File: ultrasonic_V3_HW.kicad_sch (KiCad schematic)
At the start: 7 parts, among them J1 Conn_02x20_Odd_Even, J4 Conn_01x07_Pin, J5 Screw_Terminal_01x02

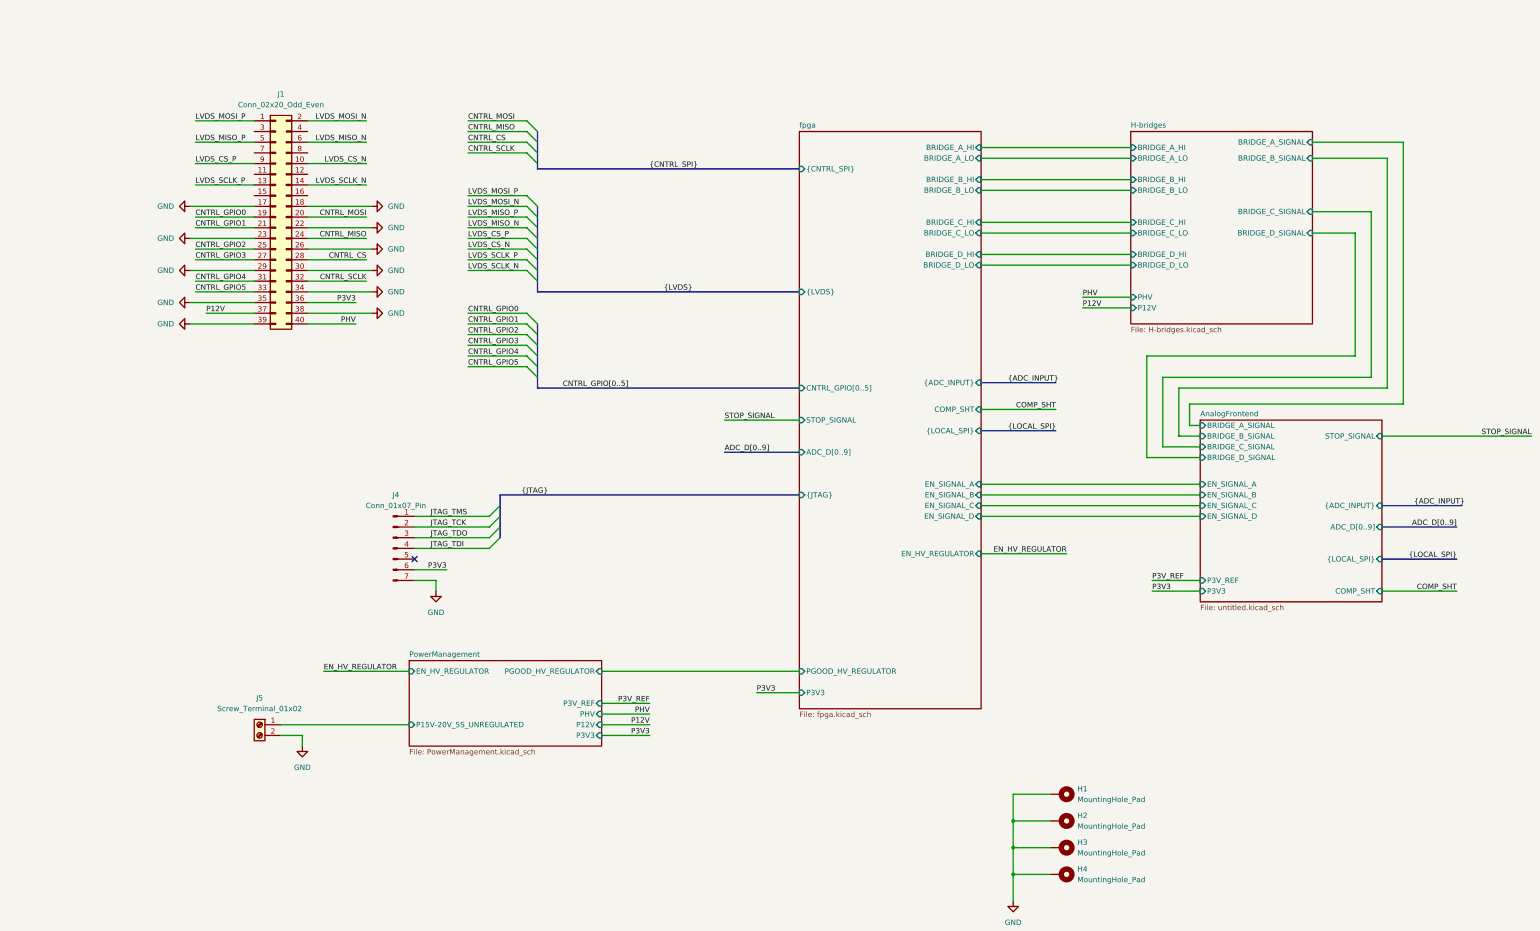
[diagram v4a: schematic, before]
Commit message: no errors schematic, basic routing done
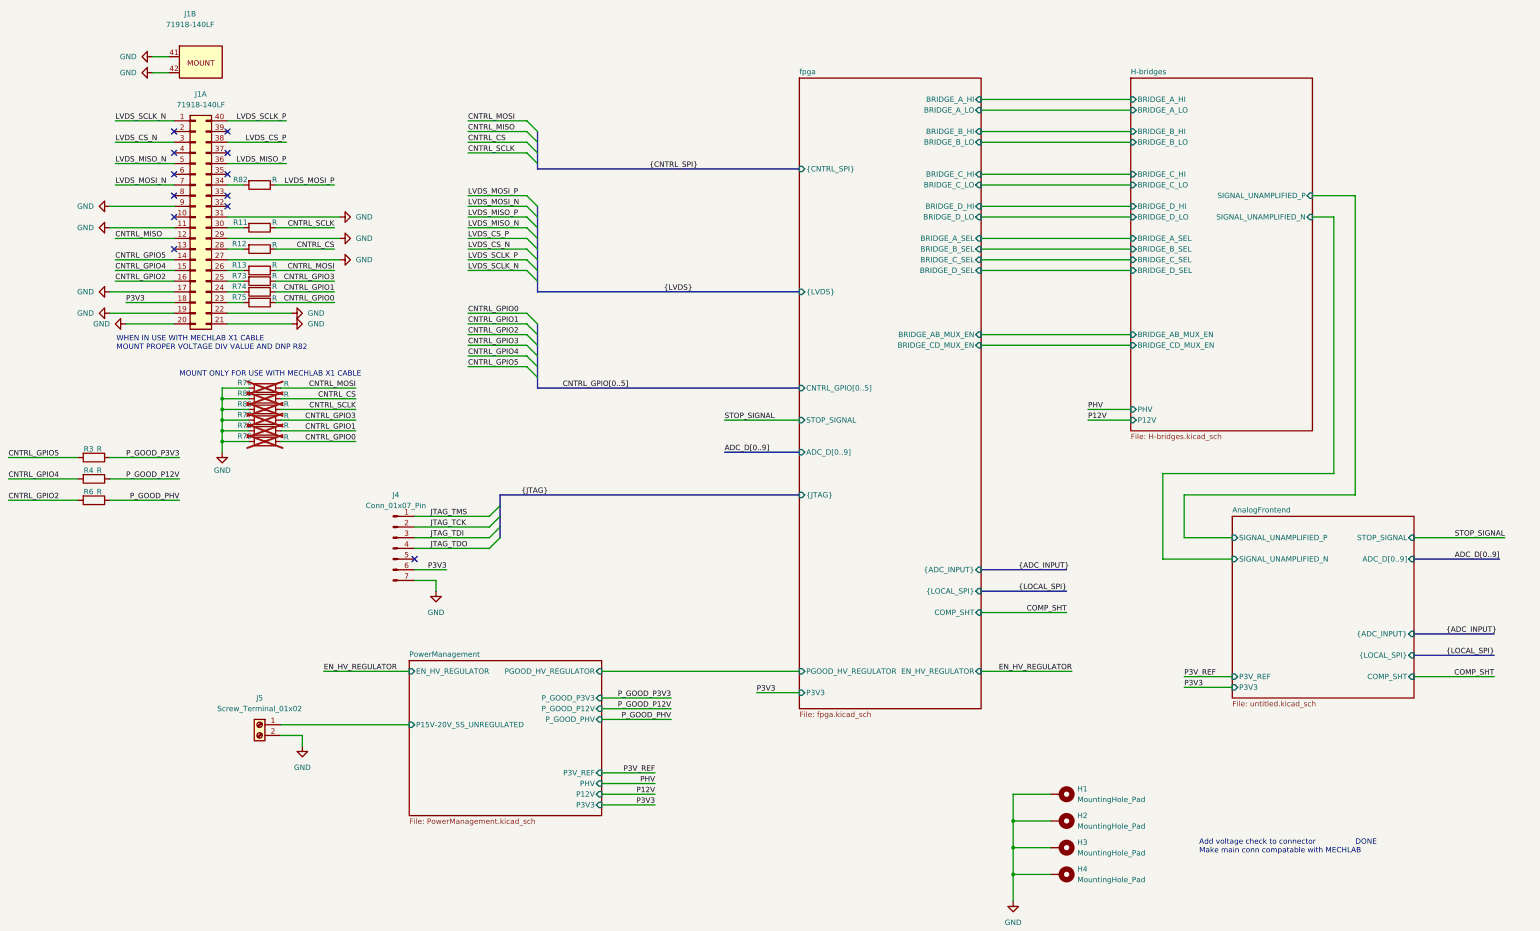
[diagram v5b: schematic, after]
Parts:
- removed J1: Conn_02x20_Odd_Even, Connector_PinHeader_2.54mm:PinHeader_2x20_P2.54mm_Vertical, symbol Connector_Generic:Conn_02x20_Odd_Even
- added J1: 71918-140LF, SpecialStuff:CON40_2X20_USZ_FCI_GLE, symbol 10_ICs:71918-140LF
- added R11, R12, R13, R3, R4, R6, R73, R74, R75, R76, R77, R78, R79, R80, R81, R82: R, Resistor_SMD:R_0603_1608Metric_Pad0.98x0.95mm_HandSolder, symbol Device:R
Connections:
- net CNTRL_CS: now also R12.1, R81.1
- net CNTRL_GPIO0: now also R75.1, R79.1
- net CNTRL_GPIO1: now also R74.1, R78.1
- net CNTRL_GPIO2: now also J1.16 (Pin_16), R6.2
- net CNTRL_GPIO3: now also R73.1, R77.1
- net CNTRL_GPIO4: now also J1.15 (Pin_15), R4.2
- net CNTRL_GPIO5: now also J1.14 (Pin_14), R3.2
- net CNTRL_MISO: now also J1.12 (Pin_12)
- net CNTRL_MOSI: now also R13.1, R76.1
- net CNTRL_SCLK: now also R11.1, R80.1
- net GND: now also J1.11 (Pin_11), J1.17 (Pin_17), J1.19 (Pin_19), J1.20 (Pin_20), J1.21 (Pin_21), J1.22 (Pin_22), J1.27 (Pin_27), J1.29 (Pin_29), J1.31 (Pin_31), J1.41 (MOUNT_HOLE), J1.42 (MOUNT_HOLE), J1.9 (Pin_9), R76.2, R77.2, R78.2, R79.2, R80.2, R81.2
- net JTAG_TDI: now also J4.3 (Pin_3); no longer J4.4 (Pin_4)
- net JTAG_TDO: now also J4.4 (Pin_4); no longer J4.3 (Pin_3)
- net LVDS_CS_N: now also J1.3 (Pin_3)
- net LVDS_CS_P: now also J1.38 (Pin_38)
- net LVDS_MISO_N: now also J1.5 (Pin_5)
- net LVDS_MISO_P: now also J1.36 (Pin_36)
- net LVDS_MOSI_N: now also J1.7 (Pin_7)
- net LVDS_MOSI_P: now also R82.1
- net LVDS_SCLK_N: now also J1.1 (Pin_1)
- net LVDS_SCLK_P: now also J1.40 (Pin_40)
- net P3V3: now also J1.18 (Pin_18)
- new net: J1.34 (Pin_34), R82.2
- new net: J1.30 (Pin_30), R11.2
- new net: J1.26 (Pin_26), R13.2
- new net: J1.24 (Pin_24), R74.2
- new net: J1.23 (Pin_23), R75.2
- new net: J1.25 (Pin_25), R73.2
- new net: J1.28 (Pin_28), R12.2
- new net P_GOOD_P12V: R4.1
- new net P_GOOD_P3V3: R3.1
- new net P_GOOD_PHV: R6.1
- no-connect marks 1 -> 12
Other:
- sheet AnalogFrontend ports: added SIGNAL_UNAMPLIFIED_N, SIGNAL_UNAMPLIFIED_P; removed BRIDGE_A_SIGNAL, BRIDGE_B_SIGNAL, BRIDGE_C_SIGNAL, BRIDGE_D_SIGNAL, EN_SIGNAL_A, EN_SIGNAL_B, EN_SIGNAL_C, EN_SIGNAL_D
- sheet H-bridges ports: added BRIDGE_AB_MUX_EN, BRIDGE_A_SEL, BRIDGE_B_SEL, BRIDGE_CD_MUX_EN, BRIDGE_C_SEL, BRIDGE_D_SEL, SIGNAL_UNAMPLIFIED_N, SIGNAL_UNAMPLIFIED_P; removed BRIDGE_A_SIGNAL, BRIDGE_B_SIGNAL, BRIDGE_C_SIGNAL, BRIDGE_D_SIGNAL
- sheet PowerManagement ports: added P_GOOD_P12V, P_GOOD_P3V3, P_GOOD_PHV; removed none
- sheet fpga ports: added BRIDGE_AB_MUX_EN, BRIDGE_A_SEL, BRIDGE_B_SEL, BRIDGE_CD_MUX_EN, BRIDGE_C_SEL, BRIDGE_D_SEL; removed EN_SIGNAL_A, EN_SIGNAL_B, EN_SIGNAL_C, EN_SIGNAL_D
- note added: "Add voltage check to connector DONE Make main conn compatable with MECHLAB"
- note added: "MOUNT ONLY FOR USE WITH MECHLAB X1 CABLE"
- note added: "WHEN IN USE WITH MECHLAB X1 CABLE MOUNT PROPER VOLTAGE DIV VALUE AND DNP R82"

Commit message: DONE - before checking
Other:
- note added: "+"
- note added: "-"
- note added: "1Mhz"
- note added: "FPGA"
- moved on the sheet: H1, H2, H3, H4, J1A, J1B, J4, J5, R11, R12, R13, R3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

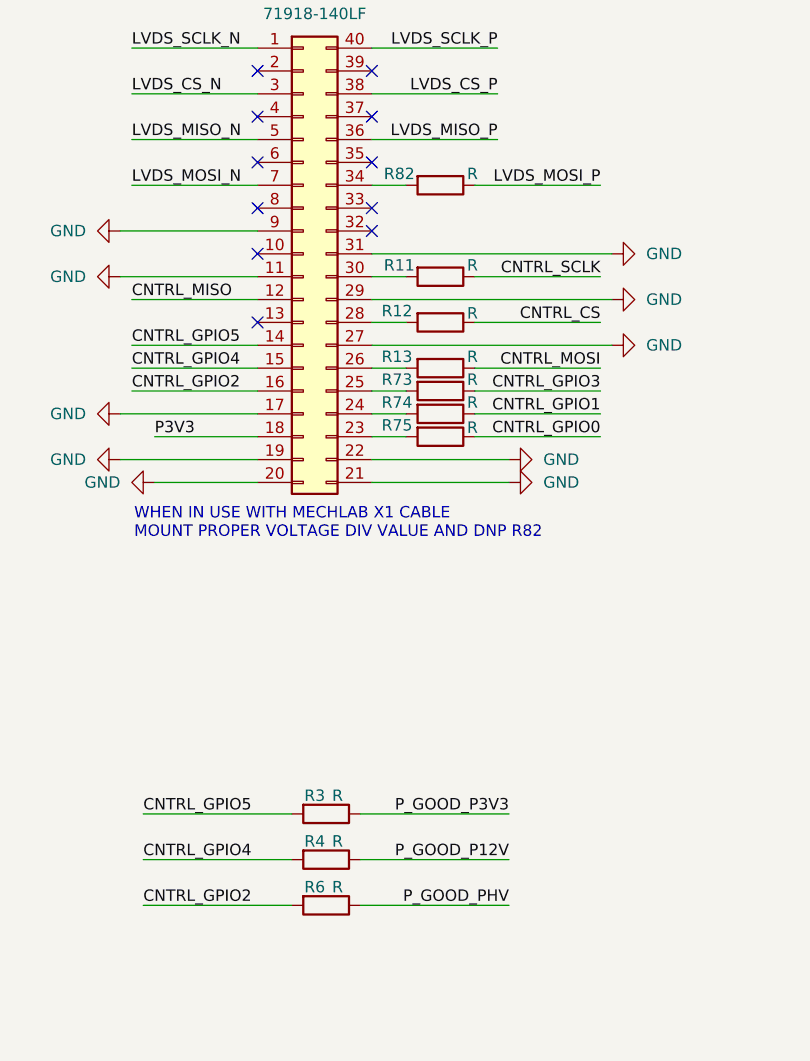
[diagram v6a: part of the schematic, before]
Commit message: most values in schematic filled corrected footprint mistake
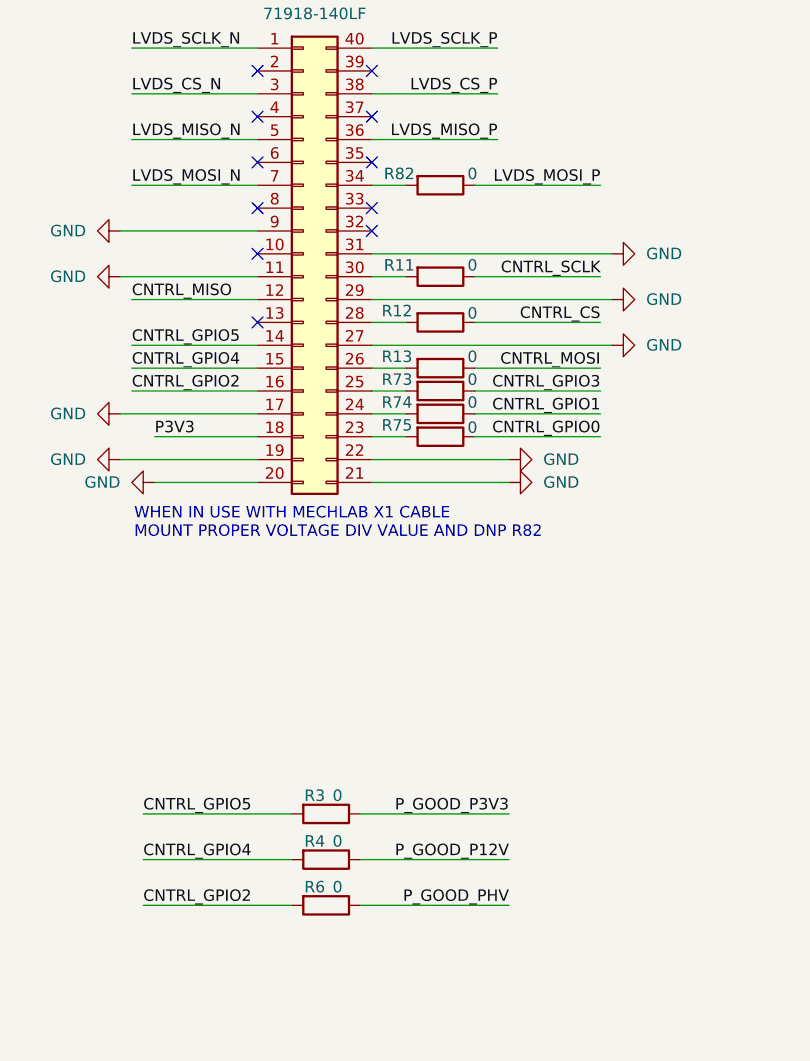
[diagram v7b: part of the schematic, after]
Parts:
- R11, R12, R13, R3, R4, R6, R73, R74, R75, R82: value R -> 0
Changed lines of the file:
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@@
 			)
 		)
-		(property "Value" "R"
+		(property "Value" "0"
 			(at 86.106 54.61 90)
 			(effects
@@
 			)
 		)
-		(property "Value" "R"
+		(property "Value" "0"
 			(at 71.12 133.858 90)
 			(effects
@@
 			)
 		)
-		(property "Value" "R"
+		(property "Value" "0"
 			(at 71.12 123.698 90)
 			(effects
@@
 			)
 		)
-		(property "Value" "R"
+		(property "Value" "0"
 			(at 86.106 64.77 90)
 			(effects
@@
 			)
 		)
-		(property "Value" "R"
+		(property "Value" "0"
 			(at 86.106 74.93 90)
 			(effects
@@
 			)
 		)
-		(property "Value" "R"
+		(property "Value" "0"
 			(at 71.12 128.778 90)
 			(effects
@@
 			)
 		)
-		(property "Value" "R"
+		(property "Value" "0"
 			(at 86.106 80.01 90)
 			(effects
@@
 			)
 		)
-		(property "Value" "R"
+		(property "Value" "0"
 			(at 86.106 77.47 90)
 			(effects
@@
 			)
 		)
-		(property "Value" "R"
+		(property "Value" "0"
 			(at 86.106 70.104 90)
 			(effects
@@
 			)
 		)
-		(property "Datasheet" "~"
+		(property "Datasheet" "https://cz.mouser.com/ProductDetail/Phoenix-Contact/1715721?qs=BYlwlsDsB%2FqgmKyTCSucHg%3D%3D"
 			(at 46.99 231.14 0)
 			(effects
@@
 			)
 		)
-		(property "Value" "R"
+		(property "Value" "0"
 			(at 86.106 82.804 90)
 			(effects

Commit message: V2 finished
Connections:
- net GND: now also J5.1 (Pin_1); no longer J5.2 (Pin_2)
- net PowerManagement/P15V-20V_5S_UNREGULATED: now also J5.2 (Pin_2); no longer J5.1 (Pin_1)
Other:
- sheet AnalogFrontend ports: added CHARGE_AMP_SHT, P12V, P3V3_A_EN; removed P3V_REF
- sheet PowerManagement ports: added none; removed P3V_REF
- sheet fpga ports: added CHARGE_AMP_SHT, P3V3_A_EN; removed none
- moved on the sheet: J5
